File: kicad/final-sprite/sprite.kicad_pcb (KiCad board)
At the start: 4 copper layers, 35 x 44.6 mm, 64 parts, among them J1 M20-7910442R, U1 CC430F513X, U2 LSM9DS1, U3 SPRITETCXO_TCXO_7Z, U4 DRV8837, U5 ADP5092, U6 DRV8837, U7 DRV8837, X1 SPRITEPIN_SPRITE_PIN, X2 SPRITEPIN_SPRITE_PIN

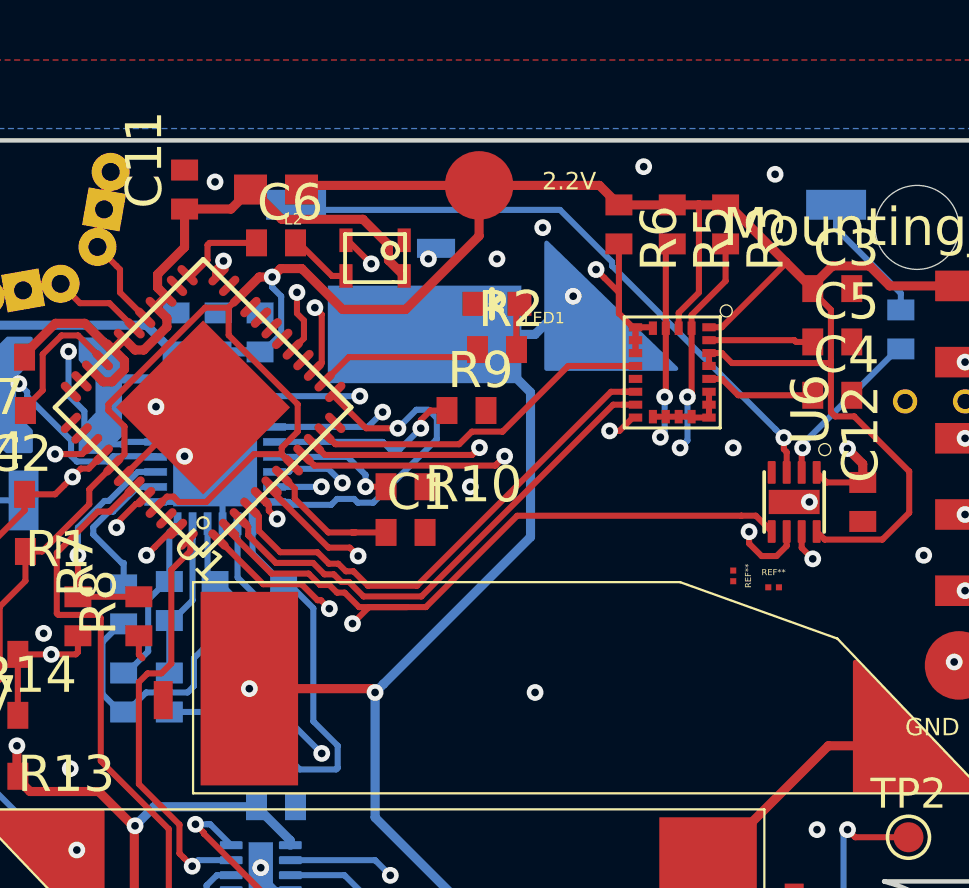
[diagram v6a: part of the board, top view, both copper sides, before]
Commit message: spiral inductor that can actually be fab'd
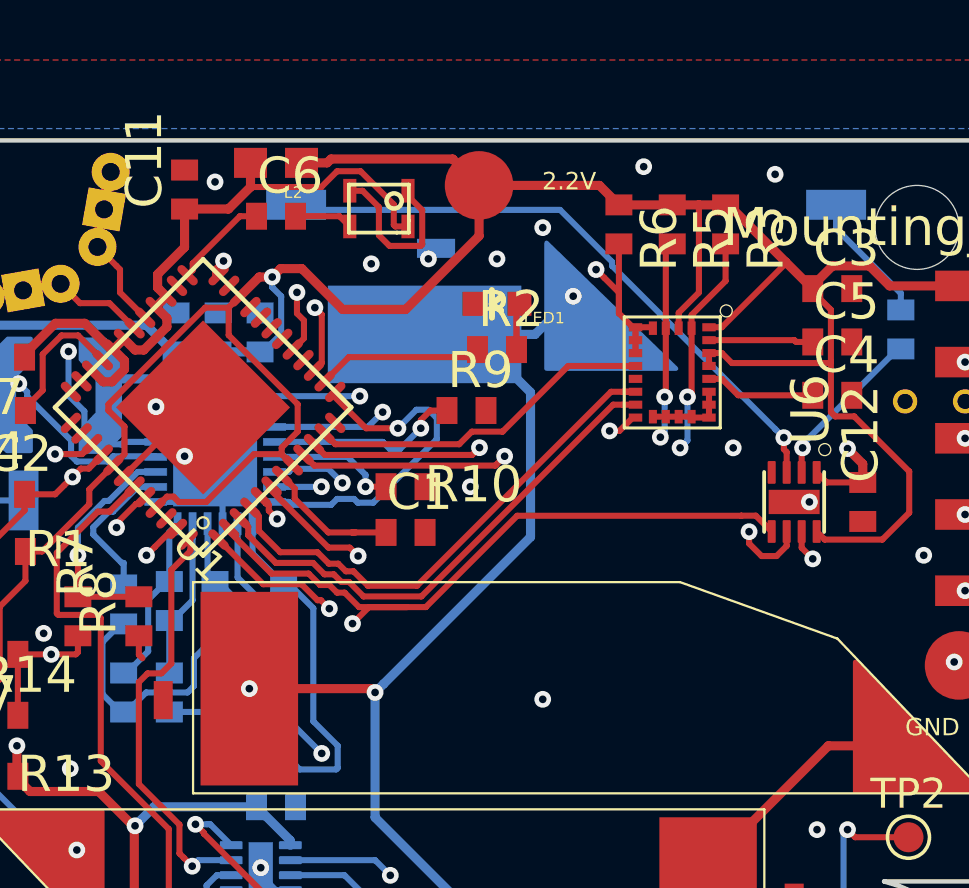
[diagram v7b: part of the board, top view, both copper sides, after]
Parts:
- removed REF** (x2): muwave_gap, muwave_gap
- moved U3 1.66 mm to (135.0, 85.7)
- moved L2 0.89 mm to (131.6, 84.2)
- moved C6 0.89 mm to (131.6, 86.0)
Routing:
- net Net-(R22-Pad1): track 186.2 -> 732.0 mm
- net GND: track 26.7 -> 31.3 mm
- net VCC: track 138.1 -> 139.5 mm
- net VCCA: track 22.3 -> 23.1 mm

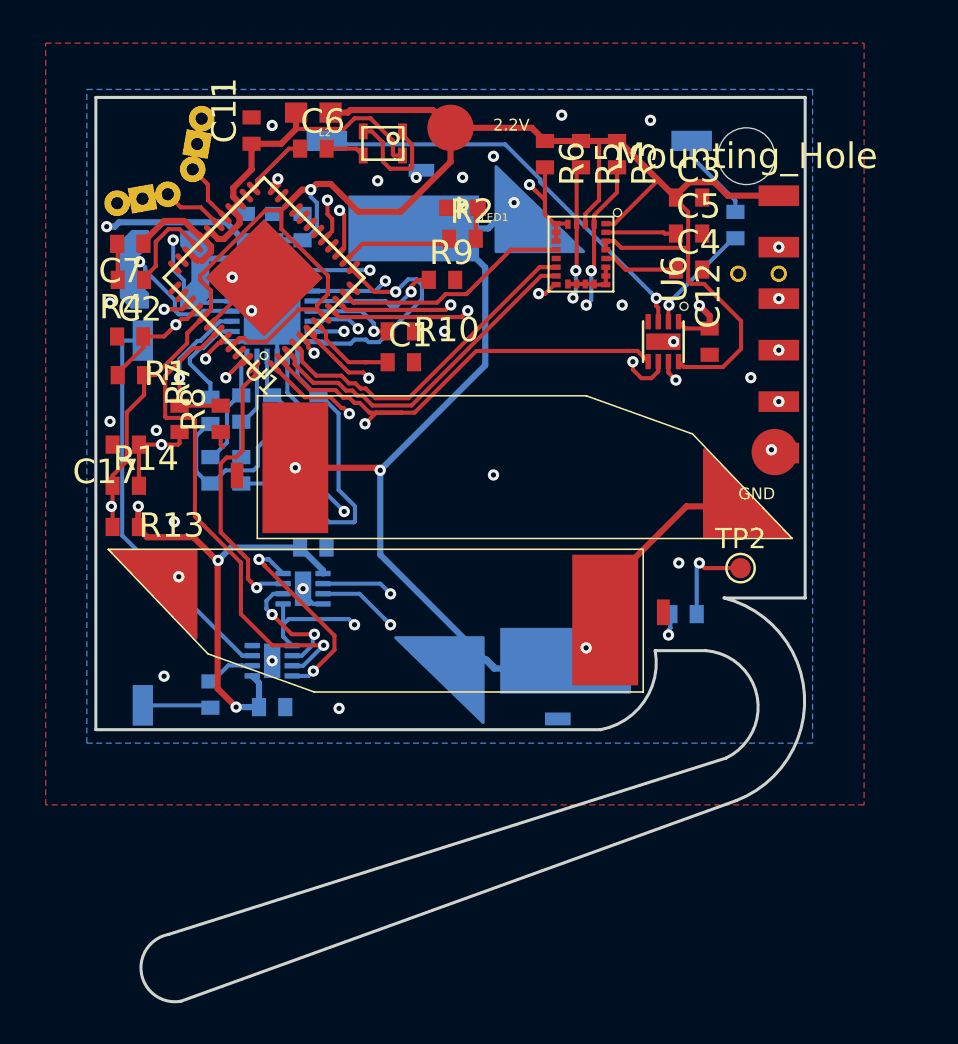
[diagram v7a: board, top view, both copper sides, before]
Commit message: Add layer 3 fill and ENIG note
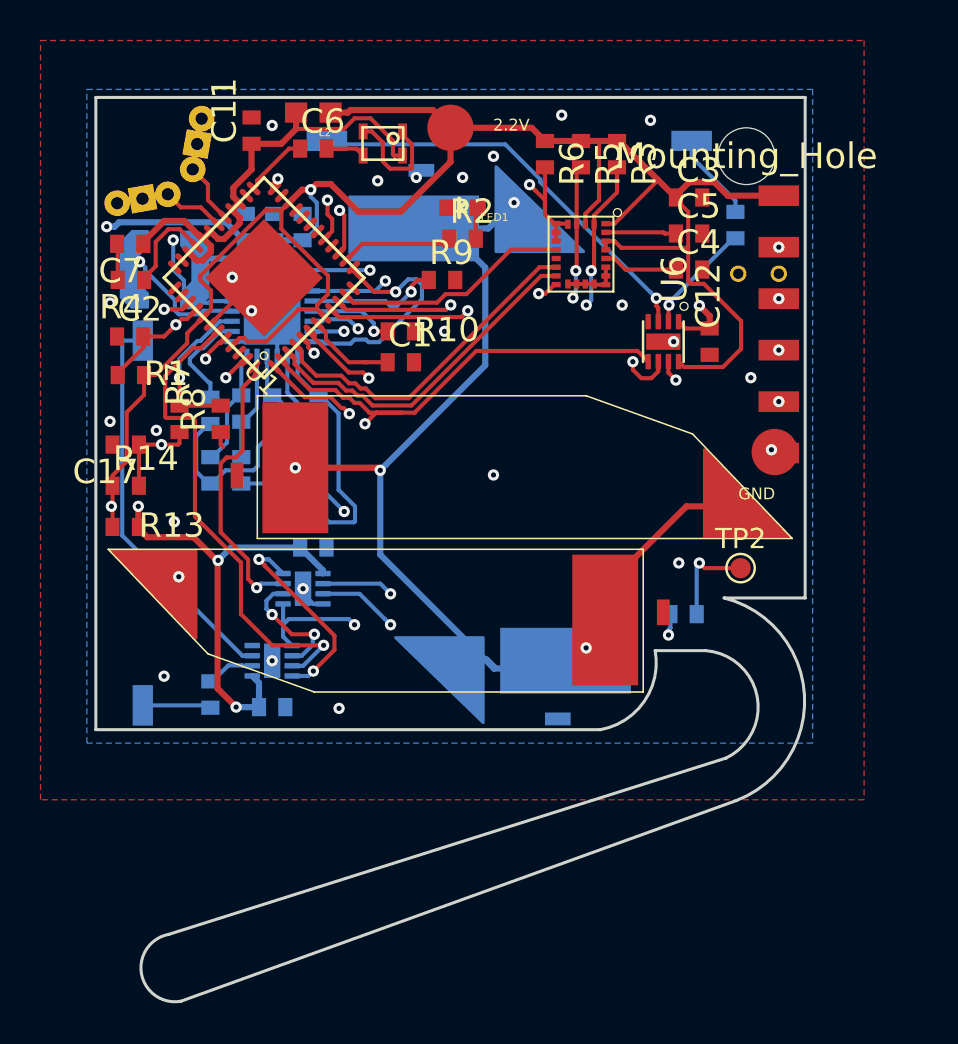
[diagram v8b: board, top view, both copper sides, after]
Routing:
- added copper zone on Route3, net GND
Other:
- board text added: "STACKUP: STANDARD FR4. 31 MIL OVERALL THICKNESS. 1.5 OZ COPPER OUTER LAYERS. 1.0 OZ COPPER INNER LAYERS. FINISH: ENIG"
- board text removed: "STACKUP: STANDARD FR4. 31 MIL OVERALL THICKNESS. 1.5 OZ COPPER OUTER LAYERS. 1.0 OZ COPPER INNER LAYERS."
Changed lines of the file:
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@@
-(kicad_pcb (version 20171130) (host pcbnew 5.0.0-rc2-unknown-7b73557~65~ubuntu16.04.1)
+(kicad_pcb (version 20171130) (host pcbnew "(5.0.0-rc2-92-g9552e0272)")
   (general
     (thickness 0.7874)
@@
     (39 F.Mask user hide)
     (40 Dwgs.User user hide)
-    (41 Cmts.User user hide)
+    (41 Cmts.User user)
     (42 Eco1.User user hide)
     (43 Eco2.User user hide)
@@
   (gr_line (start 151.8411 108.152074) (end 155.8411 108.152074) (layer Edge.Cuts) (width 0.15))
   (gr_arc (start 155.321 109.1692) (end 155.321 108.1532) (angle -126.9) (layer Cmts.User) (width 0.15))
-  (gr_text "STACKUP:\nSTANDARD FR4.\n31 MIL OVERALL THICKNESS.\n1.5 OZ COPPER OUTER LAYERS.\n1.0 OZ COPPER INNER LAYERS." (at 161.544 97.536) (layer Cmts.User)
+  (gr_text "STACKUP:\nSTANDARD FR4.\n31 MIL OVERALL THICKNESS.\n1.5 OZ COPPER OUTER LAYERS.\n1.0 OZ COPPER INNER LAYERS.\n\nFINISH: ENIG" (at 161.544 97.536) (layer Cmts.User)
     (effects (font (size 1.5 1.5) (thickness 0.3)) (justify left))
   )
@@
     (polygon
       (pts
-        (xy 119.38 82.042) (xy 157.48 82.042) (xy 157.48 116.332) (xy 119.38 116.332)
+        (xy 118.745 81.28) (xy 158.115 81.28) (xy 158.115 117.475) (xy 118.745 117.475)
       )
     )
@@
     (polygon
       (pts
-        (xy 158.75 118.364) (xy 118.364 118.364) (xy 118.364 80.772) (xy 158.75 80.772)
+        (xy 158.75 118.11) (xy 118.11 118.11) (xy 118.11 80.645) (xy 158.75 80.645)
       )
     )
@@
       )
     )
+  )
+  (zone (net 2) (net_name GND) (layer Route3) (hatch edge 0.508)
+    (connect_pads (clearance 0.254))
+    (min_thickness 0.1524)
+    (fill yes (arc_segments 16) (thermal_gap 0.3048) (thermal_bridge_width 0.508))
+    (polygon
+      (pts
+        (xy 119.38 81.915) (xy 157.48 81.915) (xy 157.48 116.84) (xy 119.38 116.84)
+      )
+    )
